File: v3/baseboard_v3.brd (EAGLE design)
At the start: 100 x 80 mm, 40 parts, among them Q1 18A/40V/5mΩ, U1 MC33926, U2 MC33926

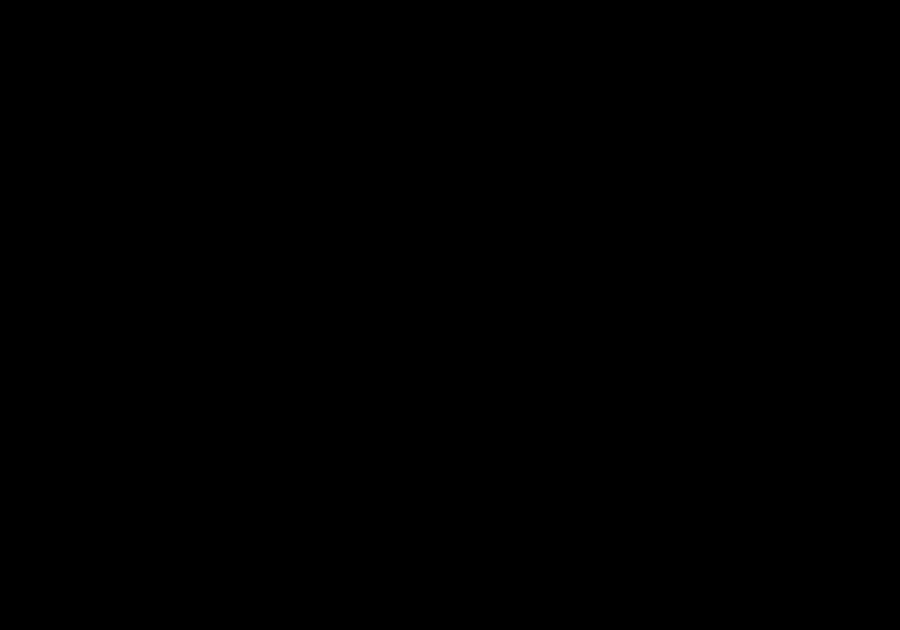
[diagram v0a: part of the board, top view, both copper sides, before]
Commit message: Adding progress on designing powerboard.
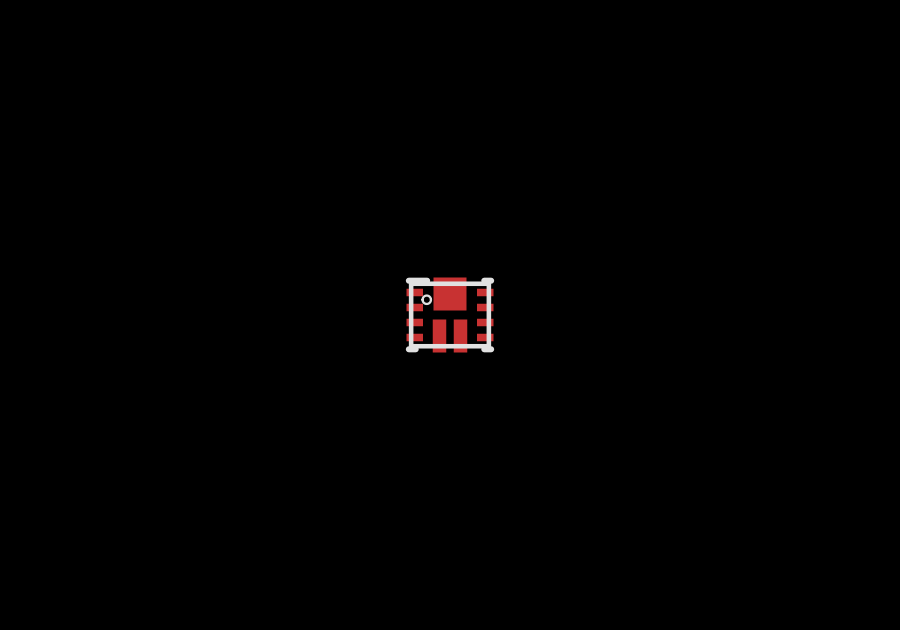
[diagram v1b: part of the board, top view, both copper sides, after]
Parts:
- added U3: Value, powerbench:RNR0011A
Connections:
- new net BOOT: U3.10
- new net GND: U3.5
- new net SW: U3.11
- new net VOUT: U3.6
- net VCC: now also U3.2
- net VIN: now also U3.9
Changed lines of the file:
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@@
 <attribute name="PROD_ID" value="CAP-00810" x="12.7" y="30.48" size="1.778" layer="27" rot="R180" display="off"/>
+</element>
+<element name="U3" library="powerbench" package="RNR0011A" value="Value" x="55.245" y="40.9575">
+<attribute name="MANUFACTURER_PART_NUMBER" value="TPS61089RNRR" x="55.245" y="40.9575" size="1.778" layer="27" display="off"/>
+<attribute name="PARTNUMBER" value="TPS61089RNRR" x="55.245" y="40.9575" size="1.778" layer="27" display="off"/>
+<attribute name="REFDES" value="RefDes" x="55.245" y="40.9575" size="1.778" layer="27" display="off"/>
+<attribute name="MANUFACTURER_NAME" value="Texas Instruments" x="55.245" y="40.9575" size="1.778" layer="27" display="off"/>
+<attribute name="TYPE" value="TYPE" x="55.245" y="40.9575" size="1.778" layer="27" display="off"/>
+<attribute name="MANUFACTURER" value="Texas Instruments" x="55.245" y="40.9575" size="1.778" layer="27" display="off"/>
 </element>
 </elements>
@@
 <via x="13.97" y="14.9225" extent="1-16" drill="0.3302"/>
 <via x="13.0175" y="14.9225" extent="1-16" drill="0.3302"/>
+<contactref element="U3" pad="9"/>
 <wire x1="19.05" y1="43.307" x2="26.67" y2="43.307" width="0" layer="19" extent="1-1"/>
 <wire x1="19.6725" y1="34.18" x2="19.05" y2="43.307" width="0" layer="19" extent="1-1"/>
@@
 <wire x1="15.025" y1="22.225" x2="11.85" y2="26.67" width="0" layer="19" extent="1-1"/>
 <wire x1="13.97" y1="18.0975" x2="15.025" y2="22.225" width="0" layer="19" extent="1-1"/>
+<wire x1="13.0175" y1="18.0975" x2="13.97" y2="18.0975" width="0" layer="19" extent="1-1"/>
+<wire x1="13.2325" y1="16.51" x2="13.0175" y2="18.0975" width="0" layer="19" extent="1-1"/>
+<wire x1="13.0175" y1="14.9225" x2="13.2325" y2="16.51" width="0" layer="19" extent="1-1"/>
+<wire x1="13.97" y1="14.9225" x2="13.0175" y2="14.9225" width="0" layer="19" extent="1-1"/>
+<wire x1="15.875" y1="15.875" x2="13.97" y2="14.9225" width="0" layer="19" extent="1-1"/>
+<wire x1="15.875" y1="16.8275" x2="15.875" y2="15.875" width="0" layer="19" extent="1-1"/>
+<wire x1="17.5725" y1="15.71" x2="15.875" y2="15.875" width="0" layer="19" extent="1-1"/>
+<wire x1="17.5725" y1="17.31" x2="17.5725" y2="15.71" width="0" layer="19" extent="1-1"/>
 <wire x1="19.6725" y1="20.21" x2="17.5725" y2="17.31" width="0" layer="19" extent="1-1"/>
 <wire x1="19.6725" y1="12.81" x2="17.5725" y2="15.71" width="0" layer="19" extent="1-1"/>
@@
 <wire x1="13.97" y1="7.747" x2="13.97" y2="14.9225" width="0" layer="19" extent="1-1"/>
 <wire x1="29.21" y1="1.69" x2="21.59" y2="7.747" width="0" layer="19" extent="1-1"/>
-<wire x1="1.27" y1="16.51" x2="13.0175" y2="14.9225" width="0" layer="19" extent="1-1"/>
+<wire x1="1.27" y1="16.51" x2="13.0175" y2="18.0975" width="0" layer="19" extent="1-1"/>
 <wire x1="32.7025" y1="21.9" x2="19.6725" y2="20.21" width="0" layer="19" extent="1-1"/>
+<wire x1="56.42" y1="41.2075" x2="13.97" y2="7.747" width="0" layer="19" extent="1-1"/>
 </signal>
 <signal name="PGND" airwireshidden="yes">
@@
 <wire x1="8.255" y1="21.59" x2="10.4775" y2="19.3675" width="0.4064" layer="16"/>
 <wire x1="10.4775" y1="19.3675" x2="10.4775" y2="14.82" width="0.4064" layer="16"/>
+<contactref element="U3" pad="2"/>
 <wire x1="8.255" y1="21.59" x2="11.01" y2="34.29" width="0" layer="19" extent="16-16"/>
+<wire x1="54.07" y1="41.2075" x2="10.4775" y2="14.82" width="0" layer="19" extent="1-16"/>
 </signal>
 <signal name="U2NSF">
@@
 <wire x1="1.27" y1="24.13" x2="4.23" y2="24.13" width="0.4064" layer="1"/>
 </signal>
+<signal name="GND">
+<contactref element="U3" pad="5"/>
+</signal>
+<signal name="VOUT">
+<contactref element="U3" pad="6"/>
+</signal>
+<signal name="BOOT">
+<contactref element="U3" pad="10"/>
+</signal>
+<signal name="SW">
+<contactref element="U3" pad="11"/>
+</signal>
 </signals>

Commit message: Moving away from bb ideas.
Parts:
- removed U3: Value, powerbench:RNR0011A
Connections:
- removed net BOOT: U3.10
- removed net GND: U3.5
- removed net SW: U3.11
- removed net VOUT: U3.6
- net VCC: no longer U3.2
- net VIN: no longer U3.9
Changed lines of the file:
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@@
 <?xml version="1.0" encoding="utf-8"?>
 <!DOCTYPE eagle SYSTEM "eagle.dtd">
-<eagle version="8.0.1">
+<eagle version="8.1.0">
 <drawing>
 <settings>
@@
 <attribute name="PROD_ID" value="CAP-00810" x="12.7" y="30.48" size="1.778" layer="27" rot="R180" display="off"/>
 </element>
-<element name="U3" library="powerbench" package="RNR0011A" value="Value" x="55.245" y="40.9575">
-<attribute name="MANUFACTURER_PART_NUMBER" value="TPS61089RNRR" x="55.245" y="40.9575" size="1.778" layer="27" display="off"/>
-<attribute name="PARTNUMBER" value="TPS61089RNRR" x="55.245" y="40.9575" size="1.778" layer="27" display="off"/>
-<attribute name="REFDES" value="RefDes" x="55.245" y="40.9575" size="1.778" layer="27" display="off"/>
-<attribute name="MANUFACTURER_NAME" value="Texas Instruments" x="55.245" y="40.9575" size="1.778" layer="27" display="off"/>
-<attribute name="TYPE" value="TYPE" x="55.245" y="40.9575" size="1.778" layer="27" display="off"/>
-<attribute name="MANUFACTURER" value="Texas Instruments" x="55.245" y="40.9575" size="1.778" layer="27" display="off"/>
-</element>
 </elements>
 <signals>
@@
 <via x="13.97" y="14.9225" extent="1-16" drill="0.3302"/>
 <via x="13.0175" y="14.9225" extent="1-16" drill="0.3302"/>
-<contactref element="U3" pad="9"/>
 <wire x1="19.05" y1="43.307" x2="26.67" y2="43.307" width="0" layer="19" extent="1-1"/>
 <wire x1="19.6725" y1="34.18" x2="19.05" y2="43.307" width="0" layer="19" extent="1-1"/>
@@
 <wire x1="1.27" y1="16.51" x2="13.0175" y2="18.0975" width="0" layer="19" extent="1-1"/>
 <wire x1="32.7025" y1="21.9" x2="19.6725" y2="20.21" width="0" layer="19" extent="1-1"/>
-<wire x1="56.42" y1="41.2075" x2="13.97" y2="7.747" width="0" layer="19" extent="1-1"/>
 </signal>
 <signal name="PGND" airwireshidden="yes">
@@
 <wire x1="8.255" y1="21.59" x2="10.4775" y2="19.3675" width="0.4064" layer="16"/>
 <wire x1="10.4775" y1="19.3675" x2="10.4775" y2="14.82" width="0.4064" layer="16"/>
-<contactref element="U3" pad="2"/>
 <wire x1="8.255" y1="21.59" x2="11.01" y2="34.29" width="0" layer="19" extent="16-16"/>
-<wire x1="54.07" y1="41.2075" x2="10.4775" y2="14.82" width="0" layer="19" extent="1-16"/>
 </signal>
 <signal name="U2NSF">
@@
 <wire x1="1.27" y1="24.13" x2="4.23" y2="24.13" width="0.4064" layer="1"/>
 </signal>
-<signal name="GND">
-<contactref element="U3" pad="5"/>
-</signal>
-<signal name="VOUT">
-<contactref element="U3" pad="6"/>
-</signal>
-<signal name="BOOT">
-<contactref element="U3" pad="10"/>
-</signal>
-<signal name="SW">
-<contactref element="U3" pad="11"/>
-</signal>
 </signals>
